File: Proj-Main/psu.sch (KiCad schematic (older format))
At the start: 111 parts, among them J1 METER, J3 T1A, J4 T1B, J5 T1C, J6 SENSE, J8 OUT+, J9 OUT-, Q1 MMBT3906, Q10 MMBT2907A, Q11 PMP4201Y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

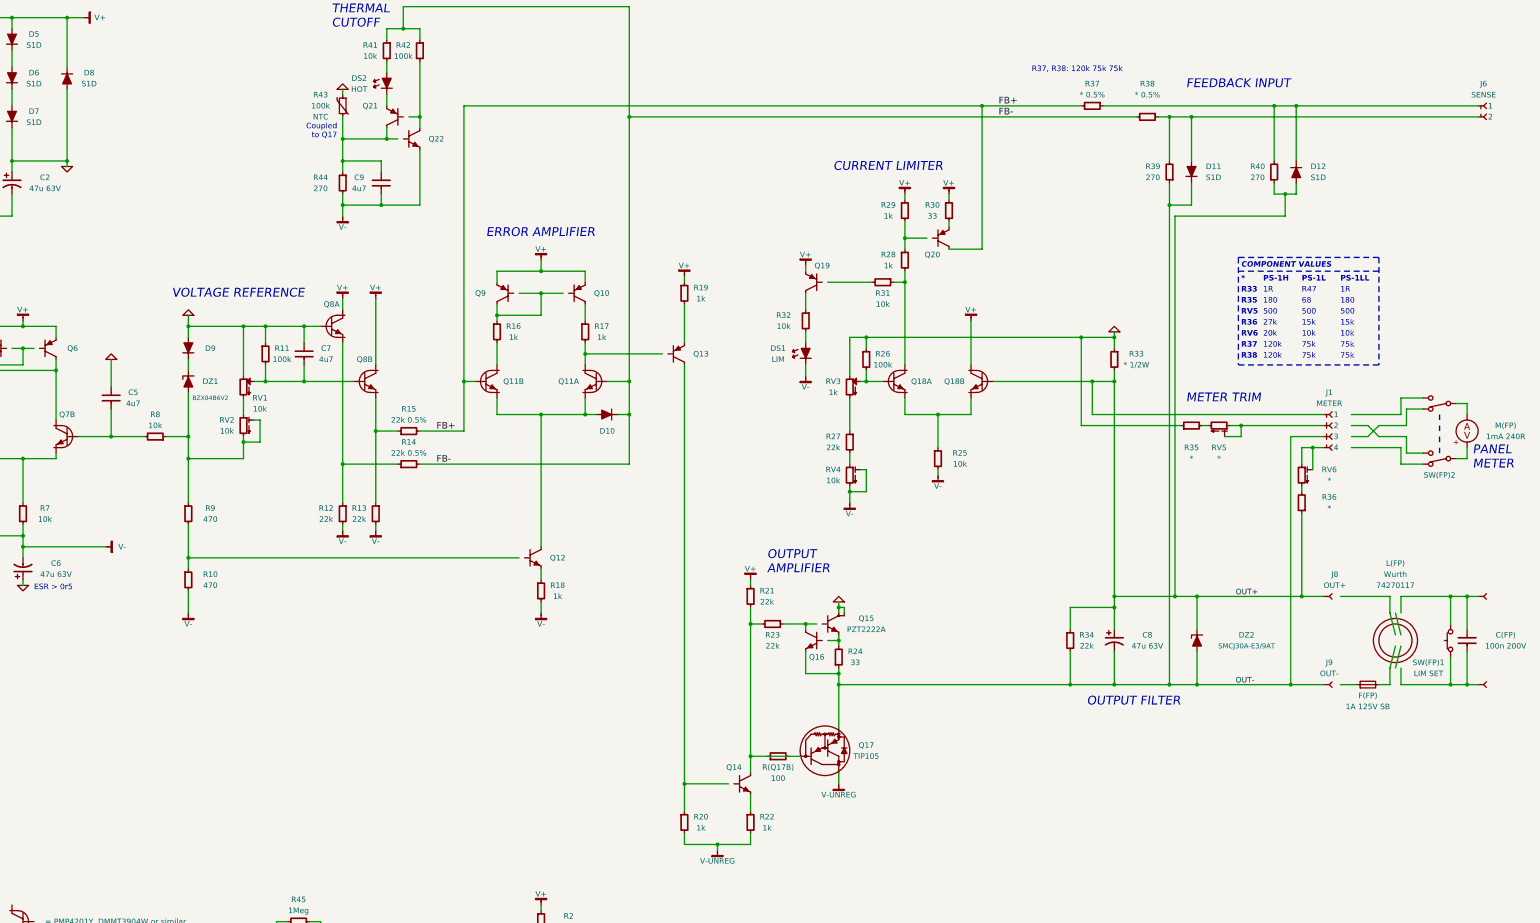
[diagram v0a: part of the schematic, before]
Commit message: Created separate wiring diagram
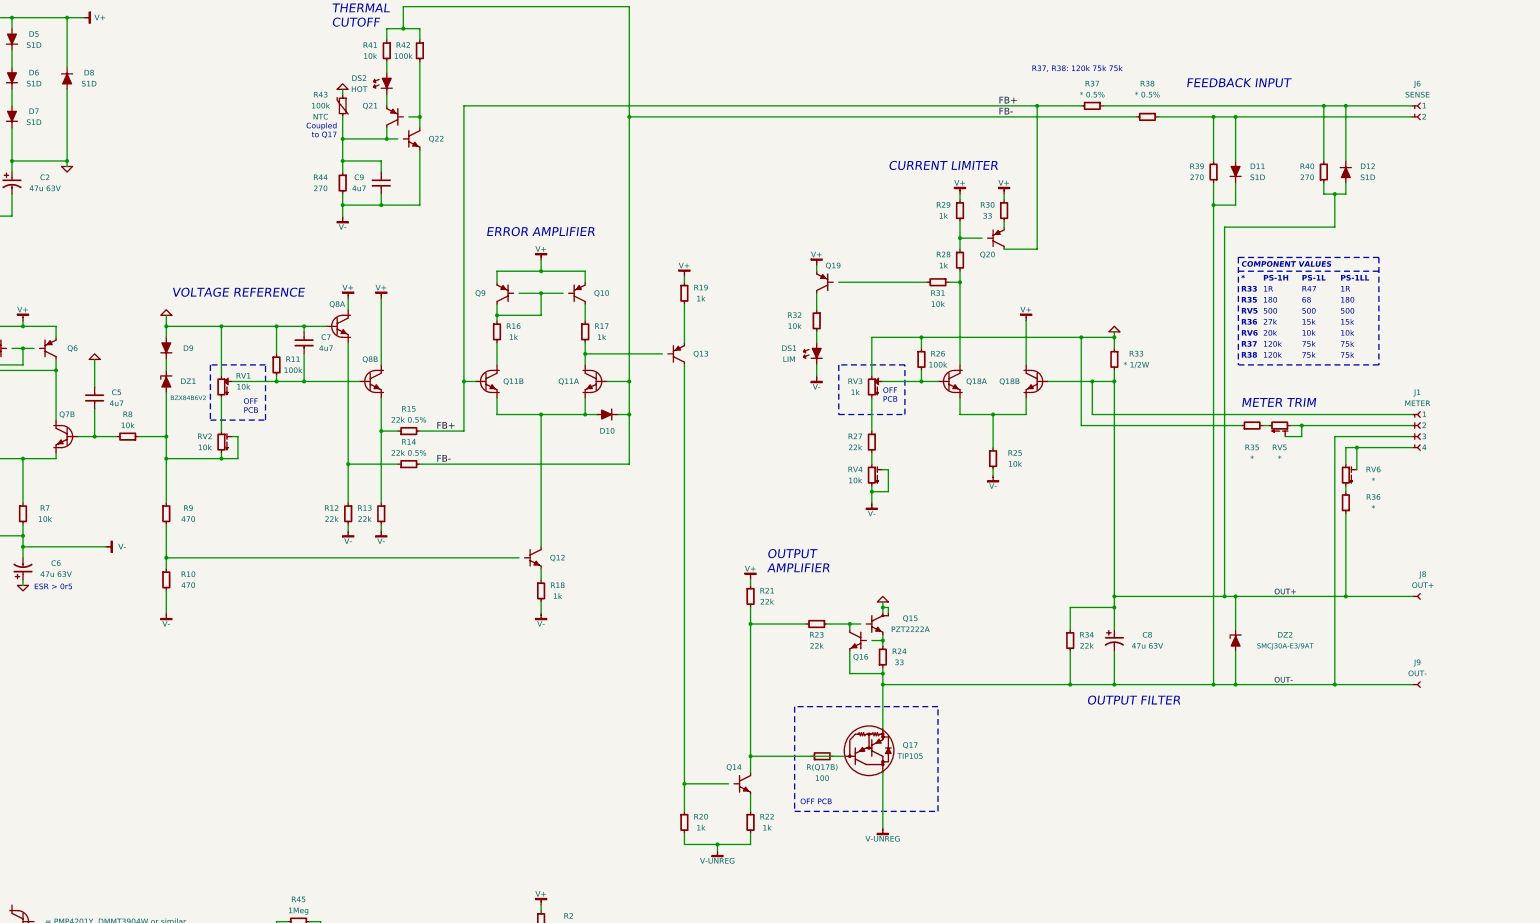
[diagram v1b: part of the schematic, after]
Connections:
- net labels removed: 100n 200V, 1A 125V SB, 1mA 240R, DPDT, LIM SET
- wire segments 292 -> 254
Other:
- note added: "OFF PCB"
- note added: "OFF\nPCB"
- note removed: "PANEL\nMETER"
- moved on the sheet: C5, C7, D11, D12, D9, DS1, DZ1, DZ2, J1, J6, J8, J9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

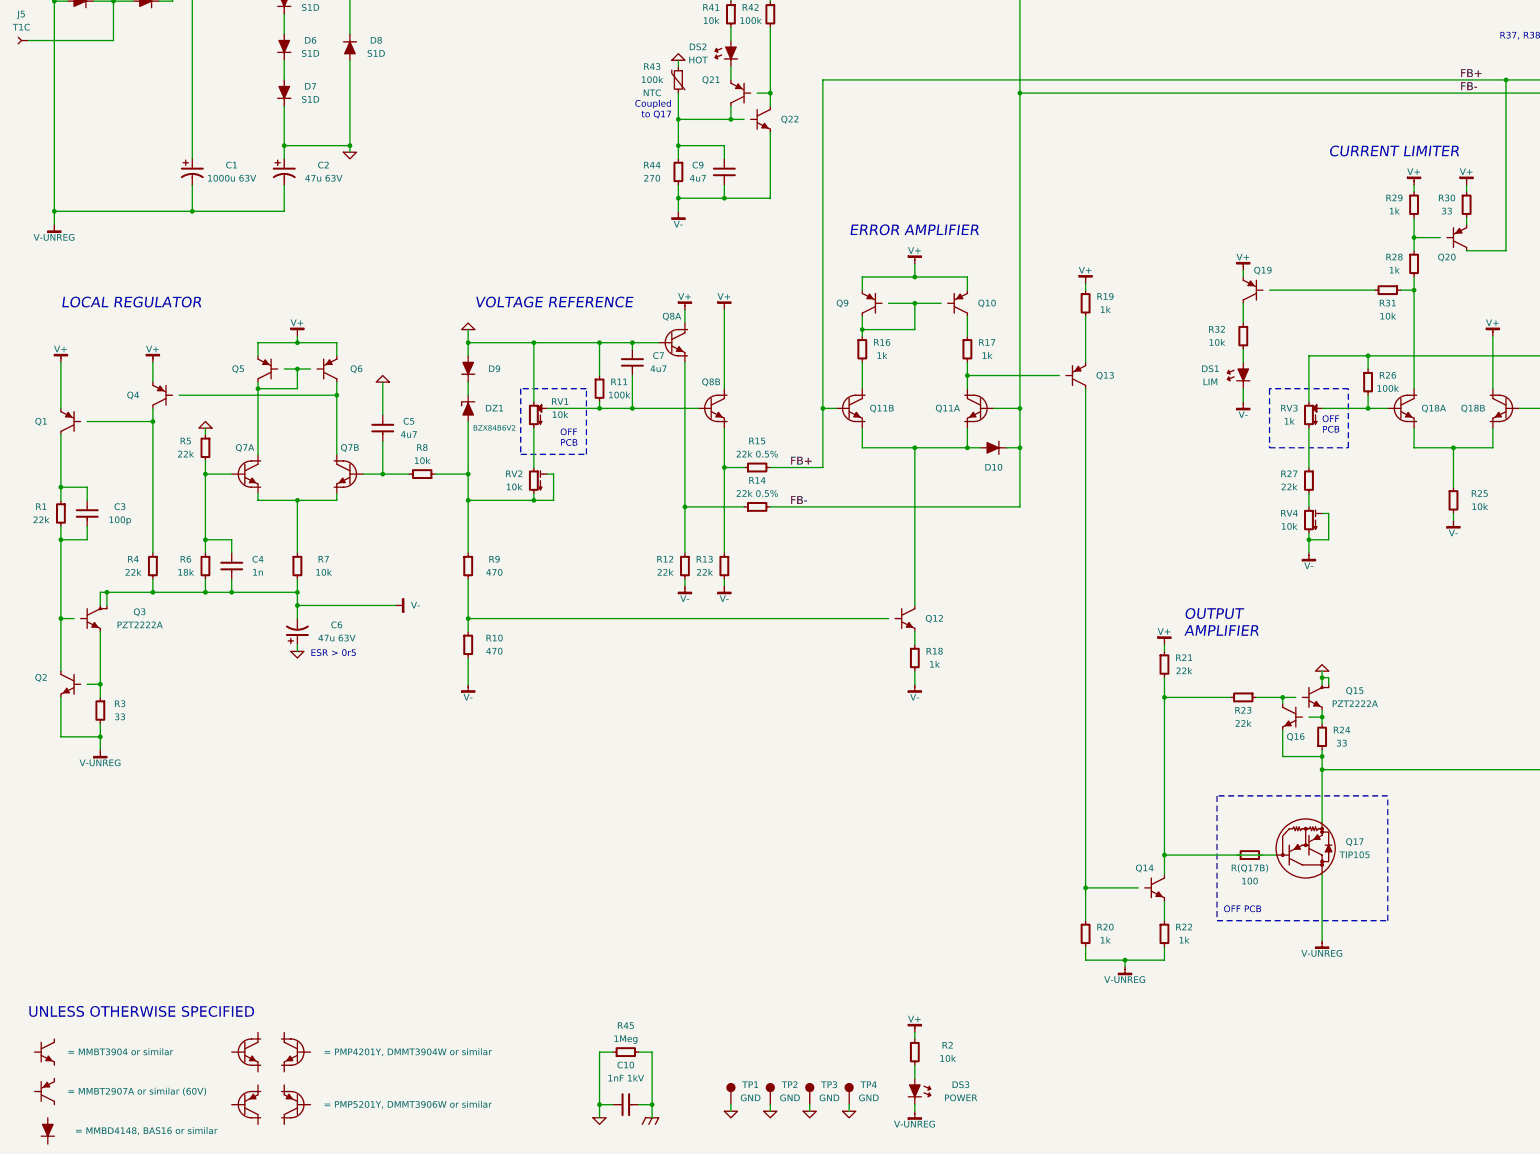
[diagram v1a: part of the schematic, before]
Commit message: Added R46, R47
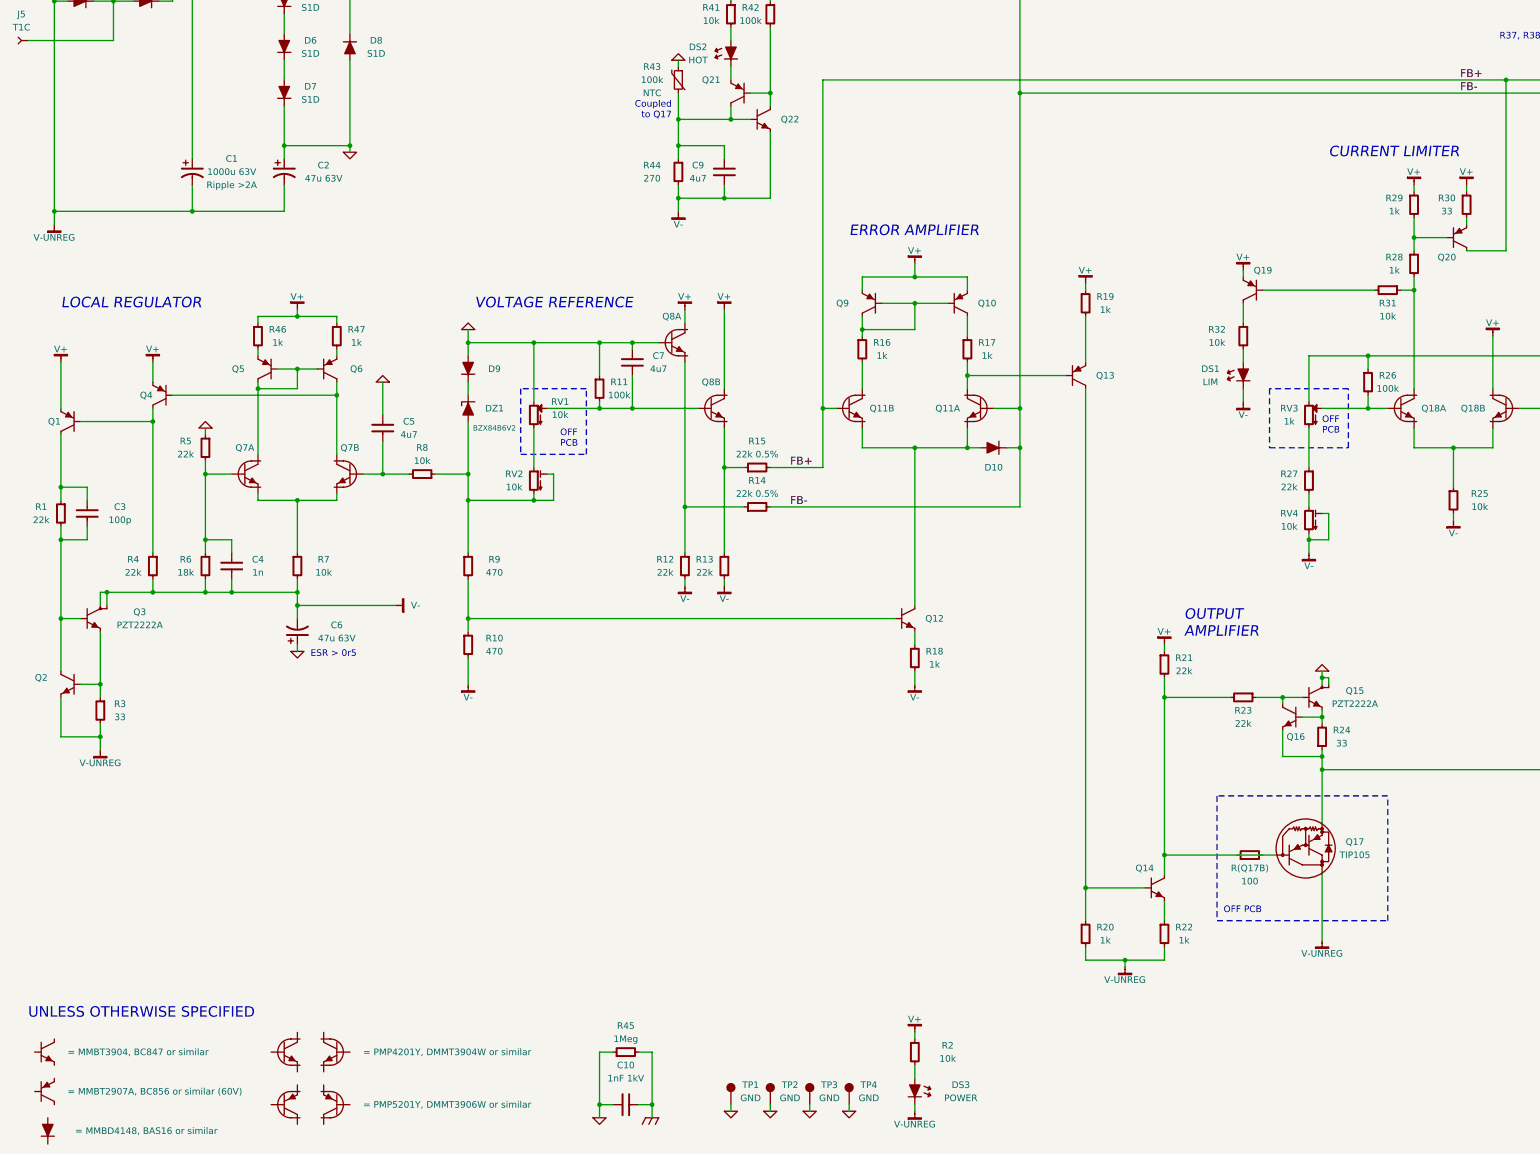
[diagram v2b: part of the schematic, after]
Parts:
- removed Q1, Q4: MMBT3906, symbol MMBT3906
- added Q1, Q4: BC856, symbol BC856
- added R46, R47: 1k, symbol R-0805
- C1: Value2 (none) -> Ripple >2A
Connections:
- net labels added: = MMBT2907A, BC856 or similar (60V), = MMBT3904, BC847 or similar
- net labels removed: = MMBT2907A or similar (60V), = MMBT3904 or similar
- wire segments 254 -> 256

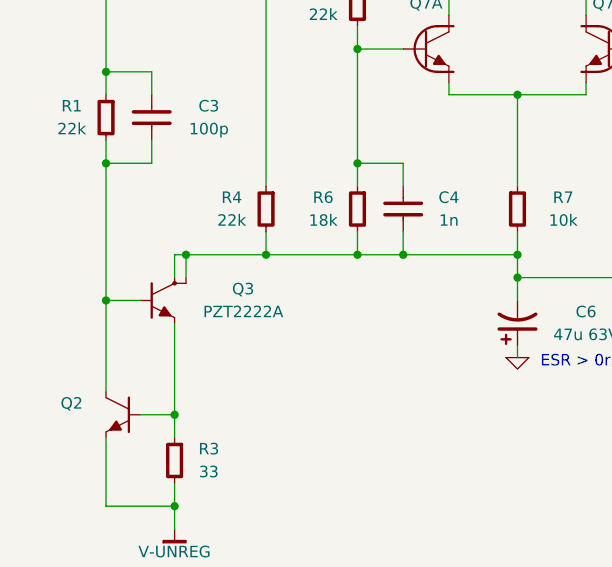
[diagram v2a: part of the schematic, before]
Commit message: Added regulator bootstrap resistor R48
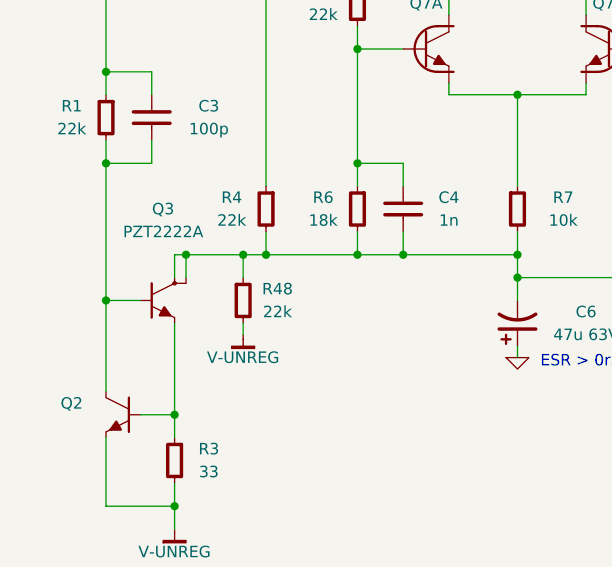
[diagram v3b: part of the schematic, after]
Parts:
- added R48: 22k, symbol R-0805
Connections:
- net V-: now also R48.1
- net V-UNREG: now also R48.2

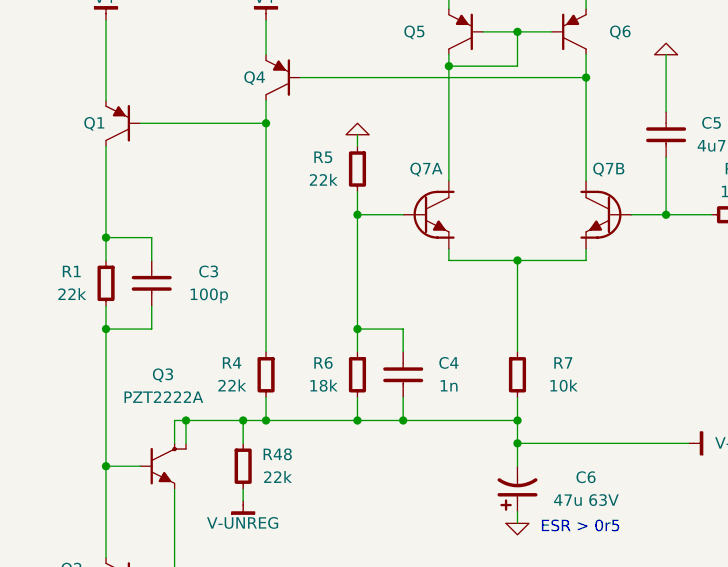
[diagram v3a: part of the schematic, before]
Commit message: Adjusted regulator feedback resistors
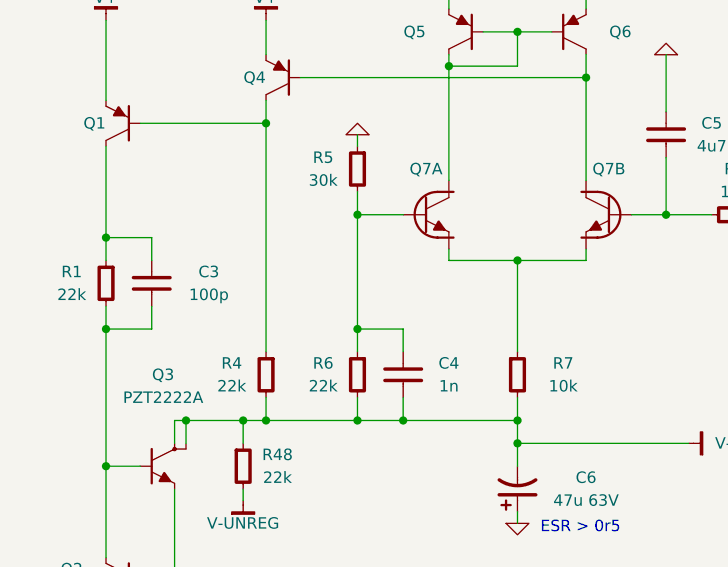
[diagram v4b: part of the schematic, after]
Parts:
- R5: value 22k -> 30k
- R6: value 18k -> 22k
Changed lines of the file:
@@
 P 2100 5900
 F 0 "R6" H 2250 5950 50  0000 C CNN
-F 1 "18k" H 2250 5850 50  0000 C CNN
+F 1 "22k" H 2250 5850 50  0000 C CNN
 F 2 "" H 2100 5950 60  0000 C CNN
 F 3 "" H 2100 5950 60  0000 C CNN
@@
 P 2100 5000
 F 0 "R5" H 2250 5050 50  0000 C CNN
-F 1 "22k" H 2250 4950 50  0000 C CNN
+F 1 "30k" H 2250 4950 50  0000 C CNN
 F 2 "" H 2100 5050 60  0000 C CNN
 F 3 "" H 2100 5050 60  0000 C CNN
